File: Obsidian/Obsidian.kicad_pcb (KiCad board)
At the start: 8 copper layers, 125 x 100 mm, 492 parts, among them J1 TYCO_1888247-1, J12 TYCO_1888247-1, J14 Conn_02x06_Top_Bottom, J15 Conn_02x06_Top_Bottom, J16 Conn_01x04, J2 USB_C_Receptacle_USB2.0_16P, J3 BELFUSE_0826-1G1T-43-F, J4 Conn_02x20_Odd_Even, J6 Conn_02x06_Top_Bottom, J7 Conn_02x06_Top_Bottom, J8 2180739-1, Q1 BSS138LT1G, Q2 BSS138LT1G, Q3 BSS138LT1G, Q4 DMP3013SFV, SW1 SW_DIP_x01, SW2 SW_DIP_x01, U1 XC7A35T-CSG325, U10 TPSM863257RDXR, U11 TPSM863257RDXR, U12 LP5951MF-3.0/NOPB, U13 LM336M-2.5, U14 DAC8550IDGK, U15 DAC8550IDGK, U16 CDCM61004RHB, U17 TCA9555RTWR, U18 TLV77325PDBVR, U2 MT41K512M16HA-125_E / MT41K51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, U20 RT9045AGSP / AP2303, U21 FT2232HQ, U22 93LC46B_SN, U23 LD39100PU12RY, U24 SN74LVC1G07DBV, U25 SN74LVC1G07DBV, U26 PCA9546ARGV, U27 W25Q128JVFIQ, U28 24AA256UID-I_ST, U3 Si5351A-B-GT, U4 TPSM863257RDXR, U5 TPSM863257RDXR, U6 TPSM863257RDXR, U7 RTL8211F-CG, U8 TLV62565DBV, U9 REF3012, Y1 9132S-Y25.000N33DT1J, Y2 VM53S3-25.000-2.5/-30+75, Y3 OSC_20MHZ_IQD_LFVCXO026156, Y4 XTAL_25MHZ_EPSON_TSX-3225_25.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, Y5 X503212MSB2GI, Y6 ABM8W-25.0000MHZ-8-D1X-T3

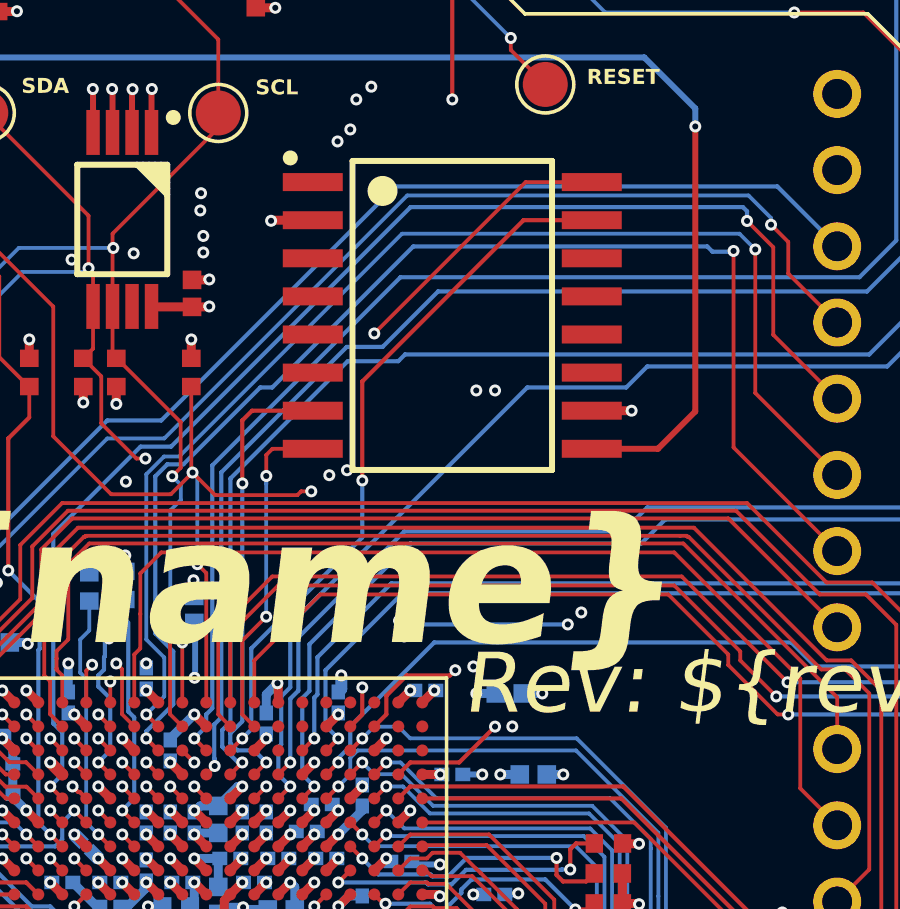
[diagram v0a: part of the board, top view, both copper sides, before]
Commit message: adding return GND for quad-spi flash
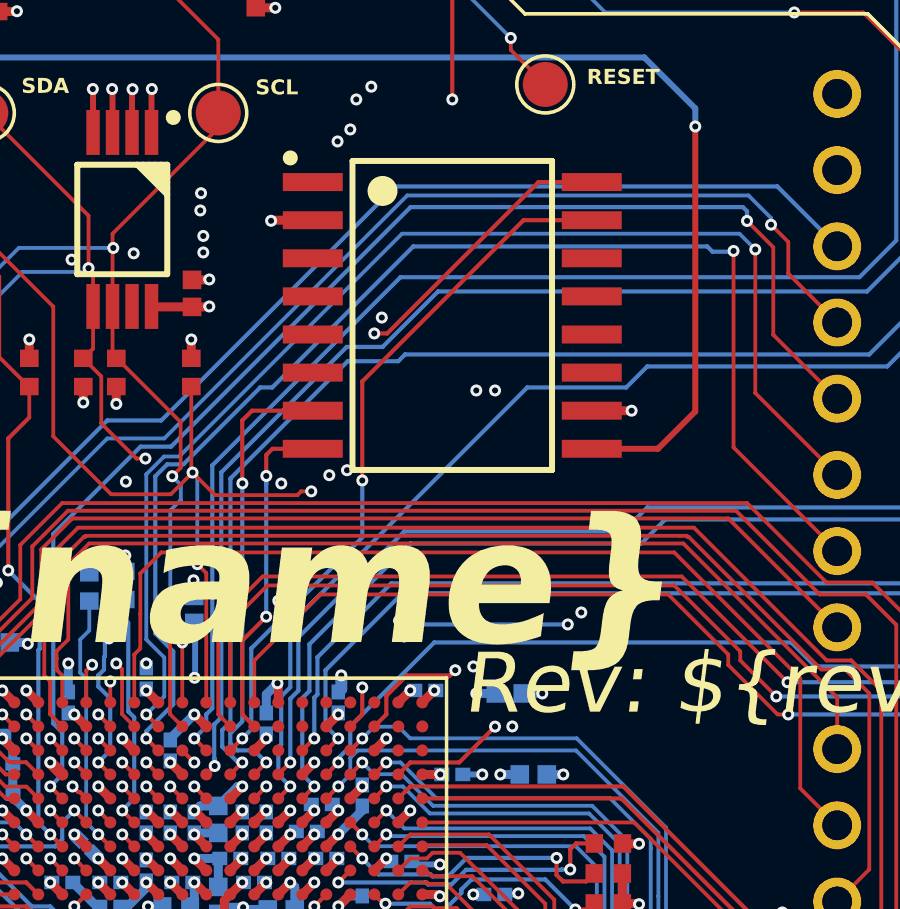
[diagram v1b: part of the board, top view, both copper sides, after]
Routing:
- net GND: vias 488 -> 491
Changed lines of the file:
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@@
 	)
 	(segment
-		(start 98.764285 76.358)
-		(end 98.764285 73.558)
+		(start 99.164285 76.758)
+		(end 98.764285 76.358)
 		(width 0.127)
 		(layer "F.Cu")
@@
 	)
 	(segment
-		(start 100.564285 71.758)
+		(start 100.244285 71.758)
 		(end 114.212033 71.758)
 		(width 0.127)
@@
 	)
 	(segment
-		(start 98.764285 73.558)
-		(end 100.564285 71.758)
+		(start 98.764285 76.358)
+		(end 98.764285 73.238)
 		(width 0.127)
 		(layer "F.Cu")
@@
 	)
 	(segment
-		(start 99.164285 76.758)
-		(end 98.764285 76.358)
+		(start 98.764285 73.238)
+		(end 100.244285 71.758)
 		(width 0.127)
 		(layer "F.Cu")
@@
 	)
 	(segment
-		(start 116.164285 74.258)
-		(end 116.164285 74.558)
+		(start 116.164285 74.558)
+		(end 117.364285 75.758)
 		(width 0.127)
 		(layer "F.Cu")
@@
 	)
 	(segment
-		(start 116.164285 74.558)
-		(end 117.364285 75.758)
+		(start 113.964285 72.058)
+		(end 116.164285 74.258)
 		(width 0.127)
 		(layer "F.Cu")
@@
 	(segment
 		(start 99.164285 75.958)
-		(end 99.164285 73.658)
+		(end 99.164285 73.298)
 		(width 0.127)
 		(layer "F.Cu")
@@
 	)
 	(segment
-		(start 113.964285 72.058)
-		(end 116.164285 74.258)
+		(start 99.164285 73.298)
+		(end 100.404285 72.058)
 		(width 0.127)
 		(layer "F.Cu")
@@
 	)
 	(segment
-		(start 99.164285 73.658)
-		(end 100.764285 72.058)
+		(start 116.164285 74.258)
+		(end 116.164285 74.558)
 		(width 0.127)
 		(layer "F.Cu")
@@
 	)
 	(segment
-		(start 100.764285 72.058)
+		(start 100.404285 72.058)
 		(end 113.964285 72.058)
 		(width 0.127)
@@
 		(start 100.569285 67.503)
 		(end 101.914285 67.503)
-		(width 0.127)
+		(width 0.14)
 		(layer "F.Cu")
 		(net 279)
@@
 		(start 99.564285 76.358)
 		(end 99.964285 76.758)
-		(width 0.127)
+		(width 0.14)
 		(layer "F.Cu")
 		(net 279)
@@
 		(start 100.364285 68.408)
 		(end 100.364285 67.708)
-		(width 0.127)
+		(width 0.14)
 		(layer "F.Cu")
 		(net 279)
@@
 		(start 100.364285 67.708)
 		(end 100.569285 67.503)
-		(width 0.127)
+		(width 0.14)
 		(layer "F.Cu")
 		(net 279)
@@
 		(start 99.564285 73.896558)
 		(end 99.564285 76.358)
-		(width 0.127)
+		(width 0.14)
 		(layer "F.Cu")
 		(net 279)
@@
 		(start 100.361285 73.099558)
 		(end 99.564285 73.896558)
-		(width 0.127)
+		(width 0.14)
 		(layer "F.Cu")
 		(net 279)
@@
 		(start 100.364285 68.6675)
 		(end 100.361285 68.6705)
-		(width 0.127)
+		(width 0.14)
 		(layer "B.Cu")
 		(net 279)
@@
 		(start 100.364285 68.408)
 		(end 100.364285 68.6675)
-		(width 0.127)
+		(width 0.14)
 		(layer "B.Cu")
 		(net 279)
@@
 		(start 100.361285 68.6705)
 		(end 100.361285 73.099558)
-		(width 0.127)
+		(width 0.14)
 		(layer "B.Cu")
 		(net 279)
@@
 	)
 	(via
+		(at 100.764285 72.568)
+		(size 0.4)
+		(drill 0.2)
+		(layers "F.Cu" "B.Cu")
+		(free yes)
+		(net 331)
+	)
+	(via
 		(at 101.964285 85.158)
 		(size 0.4)
@@
 	)
 	(via
+		(at 100.864285 68.658)
+		(size 0.4)
+		(drill 0.2)
+		(layers "F.Cu" "B.Cu")
+		(free yes)
+		(net 331)
+	)
+	(via
 		(at 103.054285 68.218)
 		(size 0.4)
@@
 	)
 	(via
+		(at 104.214285 63.128)
+		(size 0.4)
+		(drill 0.2)
+		(layers "F.Cu" "B.Cu")
+		(free yes)
+		(net 331)
+	)
+	(via
 		(at 66.764285 55.958)
 		(size 0.4)
@@
 	)
 	(segment
-		(start 94.785887 84.274202)
-		(end 94.848083 84.274202)
+		(start 111.214285 58.613)
+		(end 109.439285 58.613)
 		(width 0.14)
 		(layer "F.Cu")
@@
 	)
 	(segment
-		(start 111.214285 58.613)
-		(end 109.009285 58.613)
-		(width 0.127)
+		(start 109.439285 58.613)
+		(end 104.394285 63.658)
+		(width 0.14)
 		(layer "F.Cu")
 		(net 378)
 	)
 	(segment
-		(start 109.009285 58.613)
+		(start 104.394285 63.658)
 		(end 103.964285 63.658)
-		(width 0.127)
+		(width 0.14)
+		(layer "F.Cu")
+		(net 378)
+	)
+	(segment
+		(start 94.785887 84.274202)
+		(end 94.848083 84.274202)
+		(width 0.14)
 		(layer "F.Cu")
 		(net 378)
@@
 		(start 95.964285 80.520857)
 		(end 95.964285 80.195143)
-		(width 0.14)
+		(width 0.12)
 		(layer "In5.Cu")
 		(net 378)
@@
 		(start 99.964285 67.658)
 		(end 103.964285 63.658)
-		(width 0.14)
+		(width 0.12)
 		(layer "In5.Cu")
 		(net 378)
@@
 		(start 98.603428 79.156)
 		(end 99.403428 78.356)
-		(width 0.14)
+		(width 0.12)
 		(layer "In5.Cu")
 		(net 378)
@@
 		(start 97.003428 79.156)
 		(end 98.603428 79.156)
-		(width 0.14)
+		(width 0.12)
 		(layer "In5.Cu")
 		(net 378)
@@
 		(start 99.964285 78.120857)
 		(end 99.964285 67.658)
-		(width 0.14)
+		(width 0.12)
 		(layer "In5.Cu")
 		(net 378)
@@
 		(start 95.964285 80.195143)
 		(end 96.203428 79.956)
-		(width 0.14)
+		(width 0.12)
 		(layer "In5.Cu")
 		(net 378)
@@
 		(start 94.785887 84.274202)
 		(end 94.680487 84.274202)
-		(width 0.14)
+		(width 0.12)
 		(layer "In5.Cu")
 		(net 378)
@@
 		(start 96.529142 79.956)
 		(end 96.766285 79.718857)
-		(width 0.14)
+		(width 0.12)
 		(layer "In5.Cu")
 		(net 378)
@@
 		(start 94.680487 84.274202)
 		(end 94.366285 83.96)
-		(width 0.14)
+		(width 0.12)
 		(layer "In5.Cu")
 		(net 378)
@@
 		(start 94.366285 80.993143)
 		(end 94.601428 80.758)
-		(width 0.14)
+		(width 0.12)
 		(layer "In5.Cu")
 		(net 378)
@@
 		(start 96.203428 79.956)
 		(end 96.529142 79.956)
-		(width 0.14)
+		(width 0.12)
 		(layer "In5.Cu")
 		(net 378)
@@
 		(start 95.727142 80.758)
 		(end 95.964285 80.520857)
-		(width 0.14)
+		(width 0.12)
 		(layer "In5.Cu")
 		(net 378)
@@
 		(start 99.403428 78.356)
 		(end 99.729142 78.356)
-		(width 0.14)
+		(width 0.12)
 		(layer "In5.Cu")
 		(net 378)
@@
 		(start 99.729142 78.356)
 		(end 99.964285 78.120857)
-		(width 0.14)
+		(width 0.12)
 		(layer "In5.Cu")
 		(net 378)
@@
 		(start 96.766285 79.393143)
 		(end 97.003428 79.156)
-		(width 0.14)
+		(width 0.12)
 		(layer "In5.Cu")
 		(net 378)
@@
 		(start 94.601428 80.758)
 		(end 95.727142 80.758)
-		(width 0.14)
+		(width 0.12)
 		(layer "In5.Cu")
 		(net 378)
@@
 		(start 96.766285 79.718857)
 		(end 96.766285 79.393143)
-		(width 0.14)
+		(width 0.12)
 		(layer "In5.Cu")
 		(net 378)
@@
 		(start 94.366285 83.96)
 		(end 94.366285 80.993143)
-		(width 0.14)
+		(width 0.12)
 		(layer "In5.Cu")
 		(net 378)
